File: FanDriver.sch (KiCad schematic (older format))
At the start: 9 parts

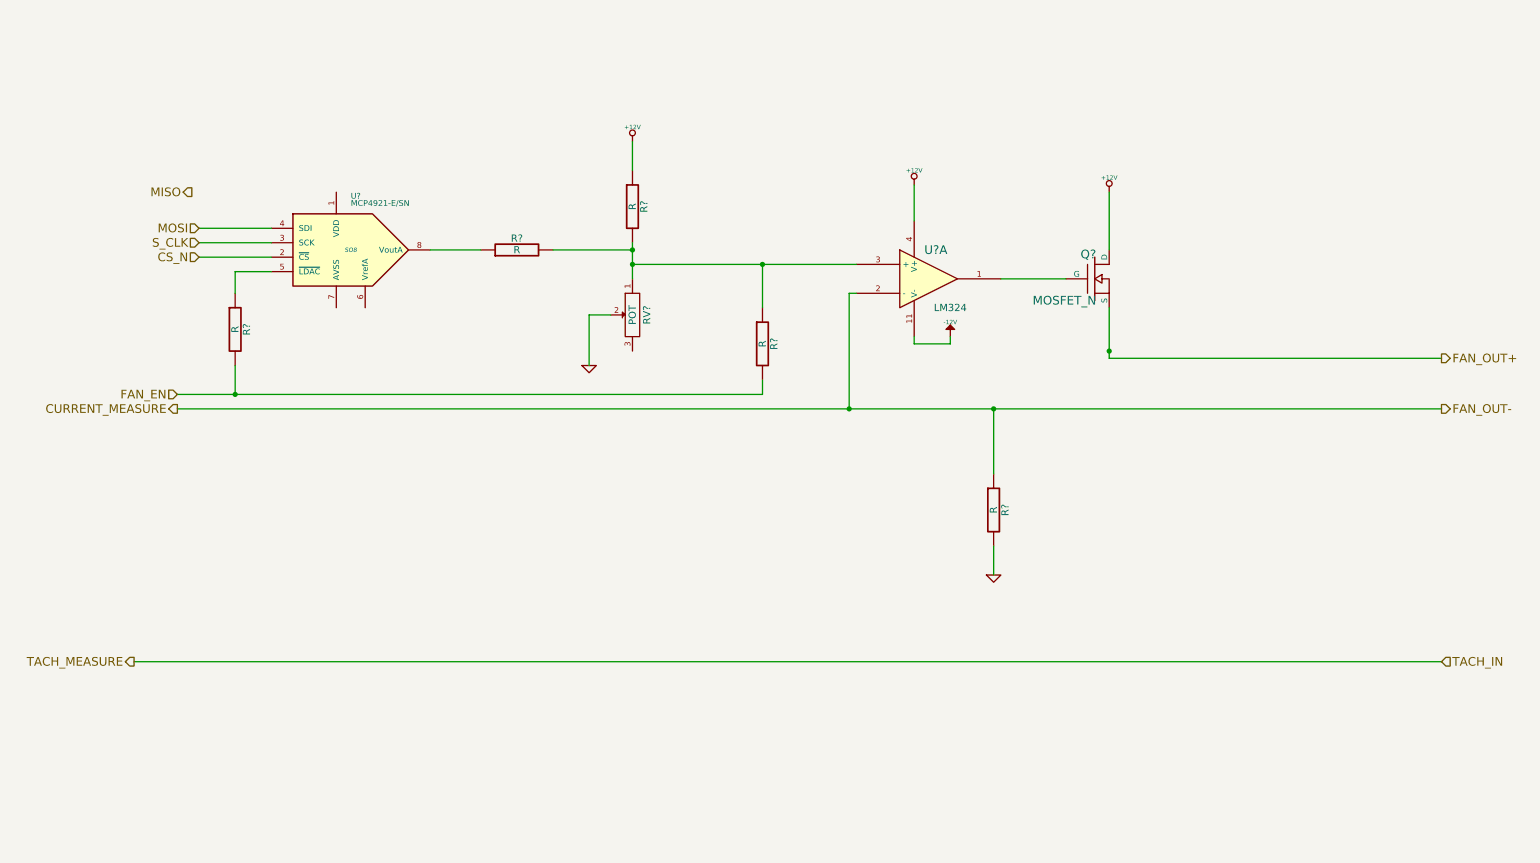
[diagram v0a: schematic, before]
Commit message: Fan/Current mode redo
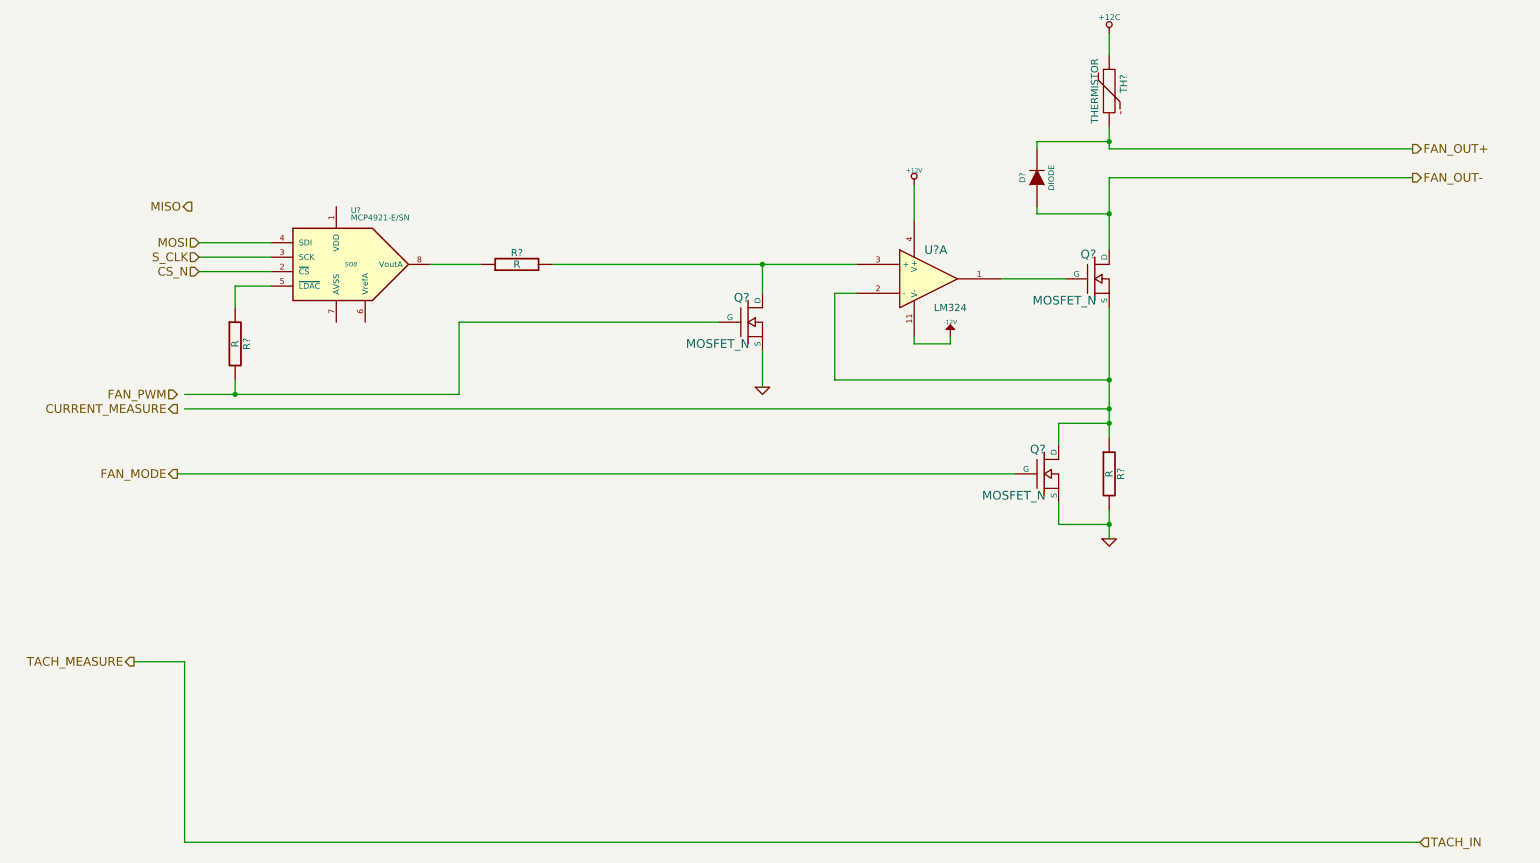
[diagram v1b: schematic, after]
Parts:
- removed R? (x2): R, symbol R
- removed RV?: POT, symbol POT
- added D?: DIODE, symbol DIODE
- added Q? (x2): MOSFET_N, symbol MOSFET_N
- added TH?: THERMISTOR, symbol THERMISTOR
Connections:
- net labels added: +12C, FAN_MODE, FAN_PWM
- net labels removed: FAN_EN
- wire segments 37 -> 41
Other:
- moved on the sheet: R?, U?
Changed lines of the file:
@@
-EESchema Schematic File Version 2  date Sat 08 Feb 2014 11:37:49 PM EST
+EESchema Schematic File Version 2  date Sun 09 Feb 2014 12:22:09 AM EST
 LIBS:power
 LIBS:device
@@
 $Descr A4 11700 8267
 encoding utf-8
-Sheet 4 9
+Sheet 3 9
 Title ""
 Date "9 feb 2014"
@@
 $EndDescr
 $Comp
+L +12C #PWR?
+U 1 1 52F70C33
+P 8400 700
+F 0 "#PWR?" H 8400 670 30  0001 C CNN
+F 1 "+12C" H 8400 810 40  0000 C CNN
+	1    8400 700
+	1    0    0    -1
+$EndComp
+Wire Wire Line
+	8400 700  8400 850
+Connection ~ 6000 2300
+Wire Wire Line
+	6000 2500 6000 2300
+Wire Wire Line
+	6000 2900 6000 3150
+Wire Wire Line
+	6650 2300 4550 2300
+Wire Wire Line
+	2000 5050 2000 6300
+Wire Wire Line
+	2000 5050 1650 5050
+Connection ~ 8400 3400
+Wire Wire Line
+	8400 3400 8050 3400
+Wire Wire Line
+	8050 3400 8050 3550
+Wire Wire Line
+	8400 3100 6500 3100
+Wire Wire Line
+	6650 2500 6500 2500
+Connection ~ 8400 1450
+Wire Wire Line
+	8400 1450 7900 1450
+Wire Wire Line
+	7900 1450 7900 1500
+Wire Wire Line
+	8400 2200 8400 1700
+Wire Wire Line
+	8400 1700 10500 1700
+Wire Wire Line
+	2600 2450 2350 2450
+Wire Wire Line
+	2350 2450 2350 2600
+Wire Wire Line
+	2100 2350 2600 2350
+Wire Wire Line
+	2100 2250 2600 2250
+Wire Wire Line
+	2100 2150 2600 2150
+Wire Wire Line
+	3700 2300 4050 2300
+Wire Wire Line
+	7050 1750 7050 2000
+Wire Wire Line
+	7650 2400 8100 2400
+Wire Wire Line
+	7050 2800 7050 2850
+Wire Wire Line
+	7050 2850 7300 2850
+Wire Wire Line
+	7300 2850 7300 2800
+Wire Wire Line
+	8400 4000 8400 4200
+Wire Wire Line
+	8400 1350 8400 1500
+Wire Wire Line
+	8400 1500 10500 1500
+Wire Wire Line
+	7900 1900 7900 1950
+Wire Wire Line
+	7900 1950 8400 1950
+Connection ~ 8400 1950
+Wire Wire Line
+	6500 2500 6500 3100
+Wire Wire Line
+	8400 3500 8400 2600
+Connection ~ 8400 3100
+Wire Wire Line
+	8400 3300 2000 3300
+Connection ~ 8400 3300
+Wire Wire Line
+	8050 3950 8050 4100
+Wire Wire Line
+	8050 4100 8400 4100
+Connection ~ 8400 4100
+Wire Wire Line
+	2000 6300 10550 6300
+Wire Wire Line
+	2350 3100 2350 3200
+Connection ~ 2350 3200
+Wire Wire Line
+	2000 3200 3900 3200
+Wire Wire Line
+	3900 3200 3900 2700
+Wire Wire Line
+	3900 2700 5700 2700
+Wire Wire Line
+	1950 3750 7750 3750
+Text HLabel 1950 3750 0    60   Output ~ 0
+FAN_MODE
+$Comp
+L MOSFET_N Q?
+U 1 1 52F70A55
+P 5900 2700
+F 0 "Q?" H 5910 2870 60  0000 R CNN
+F 1 "MOSFET_N" H 5910 2550 60  0000 R CNN
+	1    5900 2700
+	1    0    0    -1
+$EndComp
+$Comp
+L DIODE D?
+U 1 1 52F708D5
+P 7900 1700
+F 0 "D?" H 7900 1800 40  0000 C CNN
+F 1 "DIODE" H 7900 1600 40  0000 C CNN
+	1    7900 1700
+	0    -1   -1   0
+$EndComp
+$Comp
+L THERMISTOR TH?
+U 1 1 52F70886
+P 8400 1100
+F 0 "TH?" V 8500 1150 50  0000 C CNN
+F 1 "THERMISTOR" V 8300 1100 50  0000 C CNN
+	1    8400 1100
+	1    0    0    -1
+$EndComp
+$Comp
+L MOSFET_N Q?
+U 1 1 52F707B3
+P 7950 3750
+F 0 "Q?" H 7960 3920 60  0000 R CNN
+F 1 "MOSFET_N" H 7960 3600 60  0000 R CNN
+	1    7950 3750
+	1    0    0    -1
+$EndComp
+$Comp
 L GND #PWR?
 U 1 1 52F31662
-P 4800 3000
-F 0 "#PWR?" H 4800 3000 30  0001 C CNN
-F 1 "GND" H 4800 2930 30  0001 C CNN
-	1    4800 3000
-	1    0    0    -1
-$EndComp
-$Comp
-L R R?
-U 1 1 52F31643
-P 5100 1900
-F 0 "R?" V 5180 1900 50  0000 C CNN
-F 1 "R" V 5100 1900 50  0000 C CNN
-	1    5100 1900
-	1    0    0    -1
-$EndComp
-$Comp
-L POT RV?
-U 1 1 52F315F5
-P 5100 2650
-F 0 "RV?" H 5100 2550 50  0000 C CNN
-F 1 "POT" H 5100 2650 50  0000 C CNN
-	1    5100 2650
-	0    -1   1    0
-$EndComp
-$Comp
-L +12V #PWR?
-U 1 1 52F315D4
-P 5100 1450
-F 0 "#PWR?" H 5100 1400 20  0001 C CNN
-F 1 "+12V" H 5100 1550 30  0000 C CNN
-	1    5100 1450
+P 6000 3150
+F 0 "#PWR?" H 6000 3150 30  0001 C CNN
+F 1 "GND" H 6000 3080 30  0001 C CNN
+	1    6000 3150
 	1    0    0    -1
 $EndComp
@@
 L GND #PWR?
 U 1 1 52F313E3
-P 7600 4450
-F 0 "#PWR?" H 7600 4450 30  0001 C CNN
-F 1 "GND" H 7600 4380 30  0001 C CNN
-	1    7600 4450
-	1    0    0    -1
-$EndComp
-$Comp
-L +12V #PWR?
-U 1 1 52F31370
-P 8400 1800
-F 0 "#PWR?" H 8400 1750 20  0001 C CNN
-F 1 "+12V" H 8400 1900 30  0000 C CNN
-	1    8400 1800
+P 8400 4200
+F 0 "#PWR?" H 8400 4200 30  0001 C CNN
+F 1 "GND" H 8400 4130 30  0001 C CNN
+	1    8400 4200
 	1    0    0    -1
 $EndComp
@@
 $EndComp
 Text HLabel 1950 3200 0    60   Input ~ 0
-FAN_EN
+FAN_PWM
 Text HLabel 1650 5050 0    60   Output ~ 0
 TACH_MEASURE
-Text HLabel 10700 5050 2    60   Input ~ 0
+Text HLabel 10550 6300 2    60   Input ~ 0
 TACH_IN
-Text HLabel 10700 3300 2    60   Output ~ 0
+Text HLabel 10500 1700 2    60   Output ~ 0
 FAN_OUT-
-Text HLabel 10700 2950 2    60   Output ~ 0
+Text HLabel 10500 1500 2    60   Output ~ 0
 FAN_OUT+
 Text HLabel 1950 3300 0    60   Output ~ 0
@@
 L R R?
 U 1 1 52F43F3A
-P 7600 4000
-F 0 "R?" V 7680 4000 50  0000 C CNN
-F 1 "R" V 7600 4000 50  0000 C CNN
-	1    7600 4000
-	1    0    0    -1
-$EndComp
-Connection ~ 7600 3300
-Wire Wire Line
-	7600 4250 7600 4450
-Wire Wire Line
-	6600 2500 6650 2500
-Wire Wire Line
-	6600 3300 6600 2500
-Wire Wire Line
-	1950 3300 6600 3300
-Wire Wire Line
-	6600 3300 7600 3300
-Wire Wire Line
-	7600 3300 10700 3300
-Wire Wire Line
-	7600 3750 7600 3300
-Wire Wire Line
-	10700 5050 1650 5050
-Connection ~ 5100 2300
-Wire Wire Line
-	5100 2150 5100 2200
-Wire Wire Line
-	5100 2200 5100 2300
-Wire Wire Line
-	5100 2300 5100 2400
-Wire Wire Line
-	5100 1450 5100 1650
-Wire Wire Line
-	7300 2850 7300 2800
-Wire Wire Line
-	7050 2850 7300 2850
-Wire Wire Line
-	7050 2800 7050 2850
-Wire Wire Line
-	8400 2950 10700 2950
-Wire Wire Line
-	8400 2600 8400 2900
-Wire Wire Line
-	8400 2900 8400 2950
-Wire Wire Line
-	7650 2400 8100 2400
-Wire Wire Line
-	8400 1800 8400 2200
-Connection ~ 8400 2900
-Wire Wire Line
-	7050 1750 7050 2000
-Wire Wire Line
-	5100 2300 6000 2300
-Wire Wire Line
-	6000 2300 6650 2300
-Connection ~ 6600 3300
+P 8400 3750
+F 0 "R?" V 8480 3750 50  0000 C CNN
+F 1 "R" V 8400 3750 50  0000 C CNN
+	1    8400 3750
+	1    0    0    -1
+$EndComp
 $Comp
 L R R?
 U 1 1 52F4401D
-P 4300 2200
-F 0 "R?" V 4380 2200 50  0000 C CNN
-F 1 "R" V 4300 2200 50  0000 C CNN
-	1    4300 2200
+P 4300 2300
+F 0 "R?" V 4380 2300 50  0000 C CNN
+F 1 "R" V 4300 2300 50  0000 C CNN
+	1    4300 2300
 	0    -1   -1   0
 $EndComp
-Wire Wire Line
-	3700 2200 4050 2200
-Wire Wire Line
-	4550 2200 5100 2200
-Connection ~ 5100 2200
-$Comp
-L R R?
-U 1 1 52F44054
-P 6000 2850
-F 0 "R?" V 6080 2850 50  0000 C CNN
-F 1 "R" V 6000 2850 50  0000 C CNN
-	1    6000 2850
-	1    0    0    -1
-$EndComp
-Wire Wire Line
-	6000 2600 6000 2300
-Connection ~ 6000 2300
-Wire Wire Line
-	6000 3100 6000 3200
-Wire Wire Line
-	6000 3200 2350 3200
-Wire Wire Line
-	2350 3200 1950 3200
-Text HLabel 2050 1800 0    60   Output ~ 0
+Text HLabel 2050 1900 0    60   Output ~ 0
 MISO
-Text HLabel 2100 2050 0    60   Input ~ 0
+Text HLabel 2100 2150 0    60   Input ~ 0
 MOSI
+Text HLabel 2100 2350 0    60   Input ~ 0
+CS_N
 Text HLabel 2100 2250 0    60   Input ~ 0
-CS_N
-Text HLabel 2100 2150 0    60   Input ~ 0
 S_CLK
 $Comp
 L MCP4921-E/SN U?
 U 1 1 52F441DE
-P 3150 2200
-F 0 "U?" H 3150 2550 40  0000 L BNN
-F 1 "MCP4921-E/SN" H 3150 2500 40  0000 L BNN
-F 2 "SO8" H 3150 2200 30  0000 C CIN
-	1    3150 2200
-	1    0    0    -1
-$EndComp
-Wire Wire Line
-	2100 2050 2600 2050
-Wire Wire Line
-	2100 2150 2600 2150
-Wire Wire Line
-	2100 2250 2600 2250
+P 3150 2300
+F 0 "U?" H 3150 2650 40  0000 L BNN
+F 1 "MCP4921-E/SN" H 3150 2600 40  0000 L BNN
+F 2 "SO8" H 3150 2300 30  0000 C CIN
+	1    3150 2300
+	1    0    0    -1
+$EndComp
 $Comp
 L R R?
 U 1 1 52F44272
-P 2350 2750
-F 0 "R?" V 2430 2750 50  0000 C CNN
-F 1 "R" V 2350 2750 50  0000 C CNN
-	1    2350 2750
-	1    0    0    -1
-$EndComp
-Wire Wire Line
-	2350 2500 2350 2350
-Wire Wire Line
-	2350 2350 2600 2350
-Wire Wire Line
-	2350 3000 2350 3200
-Connection ~ 2350 3200
-Wire Wire Line
-	4950 2650 4800 2650
-Wire Wire Line
-	4800 2650 4800 3000
+P 2350 2850
+F 0 "R?" V 2430 2850 50  0000 C CNN
+F 1 "R" V 2350 2850 50  0000 C CNN
+	1    2350 2850
+	1    0    0    -1
+$EndComp
 $EndSCHEMATC
